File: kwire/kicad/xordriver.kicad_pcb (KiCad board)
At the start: 2 copper layers, 86.4 x 44.5 mm, 50 parts, among them J101 CONN_01X02, Q201 PMOS, Q202 NMOS, Q203 PMOS, Q204 NMOS, Q205 PMOS, Q206 NMOS, Q401 PMOS, Q402 NMOS, Q403 NMOS, Q404 PMOS, Q501 PMOS, Q502 NMOS, Q503 NMOS, Q504 PMOS, Q601 PMOS, Q602 NMOS, Q603 NMOS, Q604 PMOS, Q801 PMOS, Q802 NMOS, Q803 PMOS, Q804 NMOS, Q805 PMOS, Q806 NMOS, Q901 PMOS, Q902 NMOS, Q903 PMOS, Q904 NMOS, Q905 PMOS, Q906 NMOS

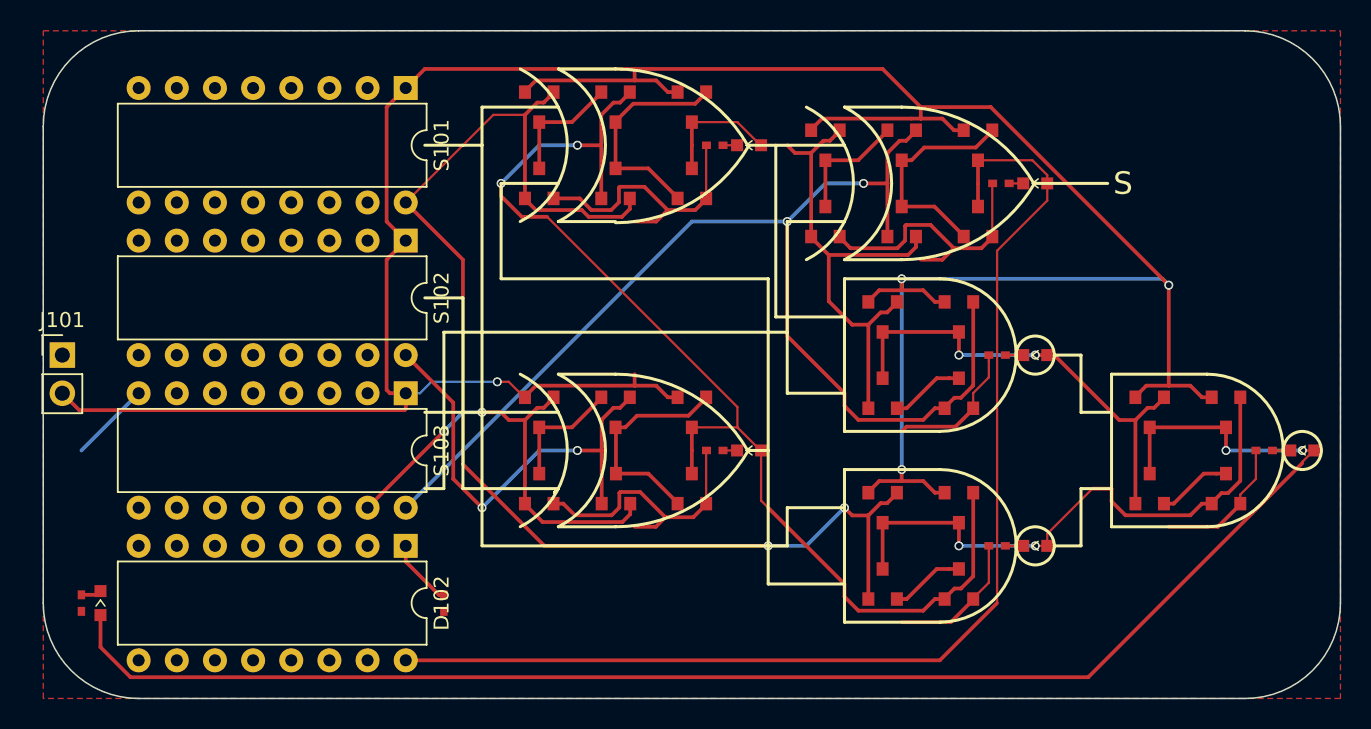
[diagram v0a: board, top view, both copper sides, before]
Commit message: Adding start for parser for kicad_pcb files
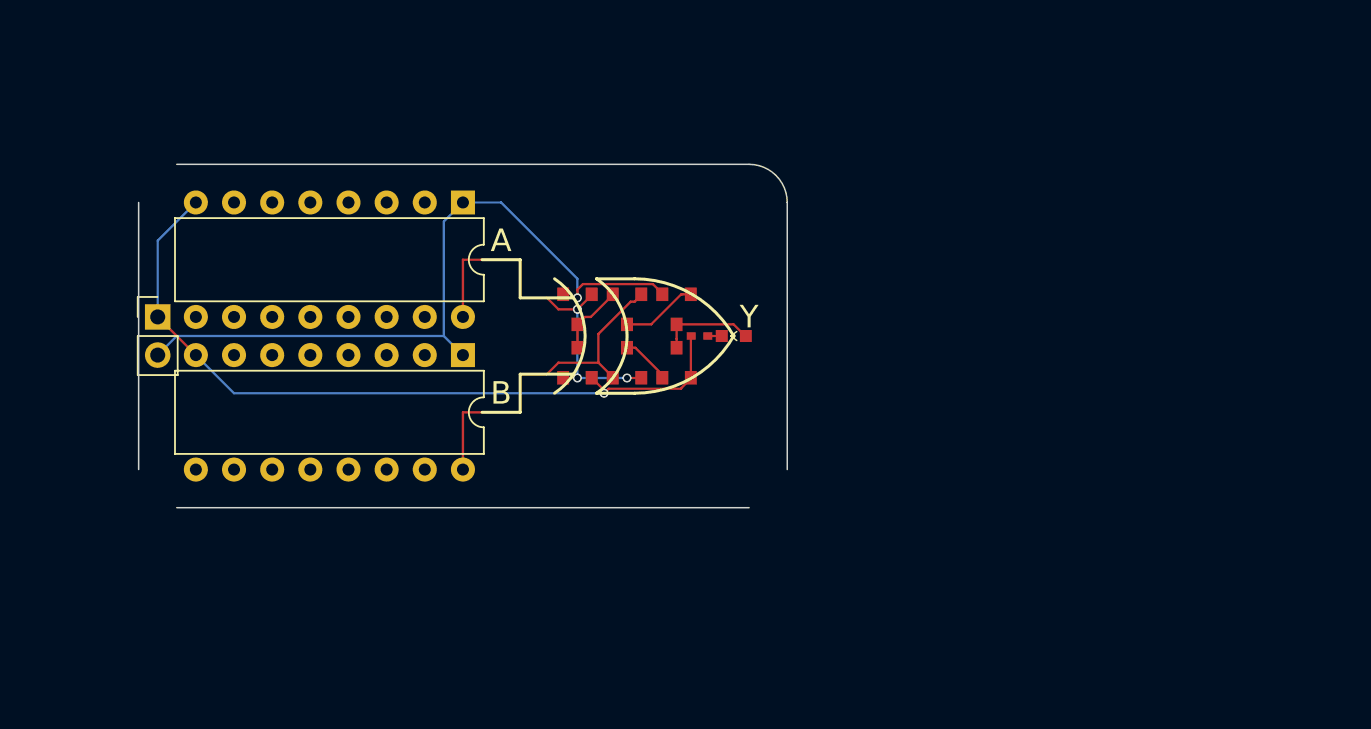
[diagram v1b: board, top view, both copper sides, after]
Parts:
- removed D101: Y, KwanSystems:D_0603
- removed D102: S, Housings_DIP:DIP-16_W7.62mm
- removed D401, D501, D601, D801, D901: LED_Small, KwanSystems:D_0603
- removed Q401, Q404, Q501, Q504, Q601, Q604, Q801, Q803, Q805, Q901, Q903, Q905: PMOS, KwanSystems:SOT-23
- removed Q402, Q403, Q502, Q503, Q602, Q603, Q802, Q804, Q806, Q902, Q904, Q906: NMOS, KwanSystems:SOT-23
- removed R101, R102, R401, R501, R601, R801, R901: RESISTOR, KwanSystems:SMD_0402
- removed S103: C, Housings_DIP:DIP-16_W7.62mm
- D201: value LED_Small -> Y
- moved Q201 13.7 mm to (105.4, 63.0)
- moved Q205 13.5 mm to (112.0, 63.0)
- moved Q203 13.5 mm to (108.7, 63.0)
- moved D201 12.7 mm to (115.8, 64.8)
- moved R201 12.7 mm to (113.5, 64.8)
- moved Q202 12.2 mm to (105.4, 66.5)
- moved Q206 12.0 mm to (112.0, 66.5)
- moved Q204 12.0 mm to (108.7, 66.5)
- moved S101 8.52 mm to (97.8, 55.9)
- moved S102 8.52 mm to (97.8, 66.0)
- moved J101 6.84 mm to (77.5, 63.5)
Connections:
- net /Y renamed /bit0/Y
- net Net-(D201-Pad1) renamed /bit0/Y-
- net Net-(Q201-Pad3) renamed /bit0/#A
- net Net-(Q203-Pad3) renamed /bit0/#Y
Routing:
- net VCC: track 204.3 -> 49.6 mm, vias 4 -> 1
- net /K: track 105.7 -> 0.00 mm, vias 2 -> 0
- net /S: track 78.9 -> 0.00 mm
- net /C: track 78.5 -> 0.00 mm, vias 2 -> 0
- net /bit0/adder/B: track 75.5 -> 0.00 mm, vias 2 -> 0
- net /A: track 84.6 -> 25.5 mm, vias 2 -> 3
- net /bit0/adder/AxorB: track 42.9 -> 0.00 mm
- net GND: track 89.8 -> 50.9 mm, vias 0 -> 1
- net /bit0/adder/#AandB: track 38.2 -> 0.00 mm, vias 2 -> 0
- net /bit0/adder/#AxorBandC: track 31.8 -> 0.00 mm, vias 2 -> 0
- net /SUB: track 29.9 -> 0.00 mm, vias 2 -> 0
- net Net-(Q803-Pad3): track 15.0 -> 0.00 mm
- net Net-(Q903-Pad3): track 14.9 -> 0.00 mm
- net Net-(Q901-Pad3): track 8.07 -> 0.00 mm
- net Net-(Q801-Pad3): track 8.07 -> 0.00 mm
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- removed copper zone on F.Cu, net GND
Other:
- board size 86.4 x 44.5 mm -> 43.2 x 22.9 mm
- board text added: "A"
- board text added: "B"
- board text added: "Y"
- board text removed: "S"

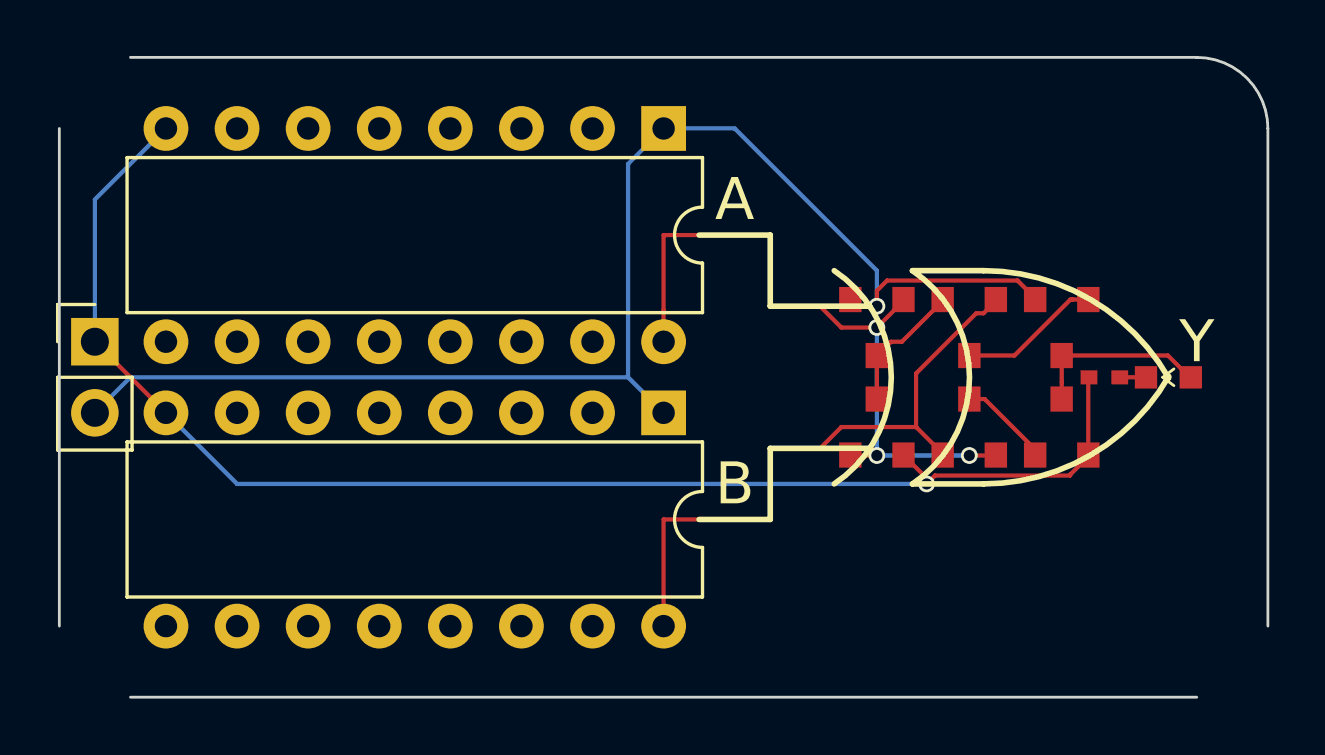
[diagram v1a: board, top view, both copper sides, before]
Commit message: Forked the XOR.
The 6-transistor XOR gate works fine, but depends on having access to the
body terminal of the transistor. In an IC, all body terminals are connected to
VCC (for PMOS) or GND (for NMOS), so that the gate voltages are relative to the
power supply rails. Therefore, you can use NMOS as a high-side switch and PMOS
as a low-side switch.

The 6T gate depends on this, because the power rails for the middle inverter are
not VCC and GND, but A and #A. When A is asserted, the middle inverter rails are
reversed from normal, and turning on the PMOS lets through low voltage instead
of the normal high voltage (and vice versa for the NMOS). You can turn on the
PMOS because the gate referenced to the body, which is tied to VCC, not to
source (and vice versa for the NMOS).

With discrete transistors, the body is always tied to the source. This means
that if you reverse the rails, you can't turn on either of the transistors,
because for the PMOS, you need the gate to be lower than the source, but the
source is low (and vice versa for the NMOS).

It is easy enough to simulate a transistor with its body wired properly -- just
ignore it. On a PMOS, the drain is set to equal the source if the gate is low,
and set to Z if the gate is high. On an NMOS, the drain is set equal to the
source if the gate is high, and Z if low.

However, a circuit built with discrete FETs won't work. As soon as the source
of the PMOS goes low, you have to hit the gate with a negative voltage (lower
than low), and as soon as the source of the NMOS goes high, you have to hit it
with a voltage higher than high.

The CD4007 chip is a set of three complementary pairs of transistors. The first
pair has its source and body pins tied to VCC and GND. The gates are connected
together and the drains are independent. The second pair has its sources
connected to pins, but its body tied to VCC and GND, respectively. The gates are
again connected together and the drains are again independent. The third pair
is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
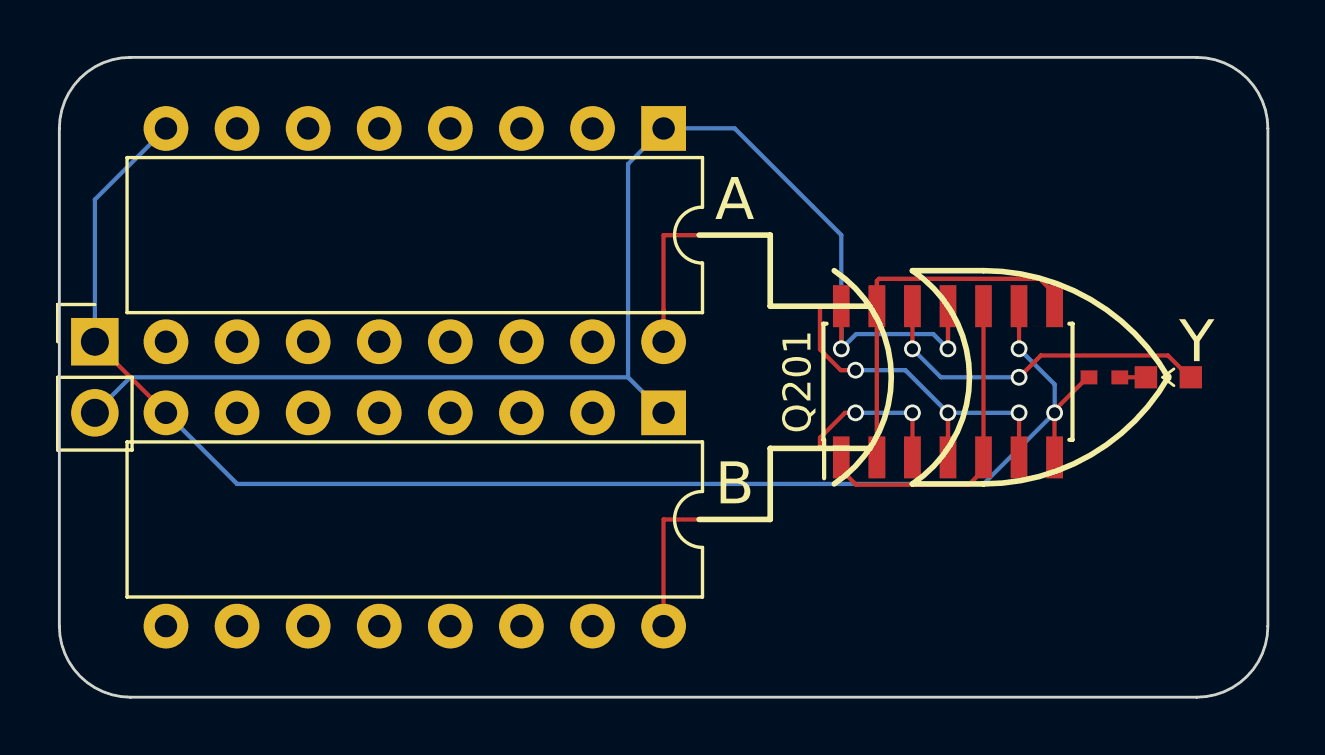
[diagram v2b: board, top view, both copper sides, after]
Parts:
- removed Q202, Q204, Q206: NMOS, KwanSystems:SOT-23
- removed Q203, Q205: PMOS, KwanSystems:SOT-23
- Q201: value PMOS -> CD4007; footprint KwanSystems:SOT-23 -> Housings_SOIC:SOIC-14_3.9x8.7mm_Pitch1.27mm
- moved Q201 3.19 mm to (108.0, 64.9), turned to 90 degrees
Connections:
- Q201 pad 1: /A -> /bit0/#Y
- Q201 pad 2: VCC -> /bit0/#A
- Q201 pad 3: /bit0/#A -> /B
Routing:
- net /bit0/#A: track 4.77 -> 13.9 mm
- net /bit0/Y: track 6.49 -> 12.5 mm, vias 0 -> 2
- net /B: track 23.0 -> 17.6 mm, vias 0 -> 2
- net GND: track 50.9 -> 53.9 mm, vias 1 -> 2
- net /bit0/#Y: track 10.1 -> 11.8 mm
- net /A: track 25.5 -> 24.8 mm
- net VCC: track 49.6 -> 50.1 mm, vias 1 -> 2

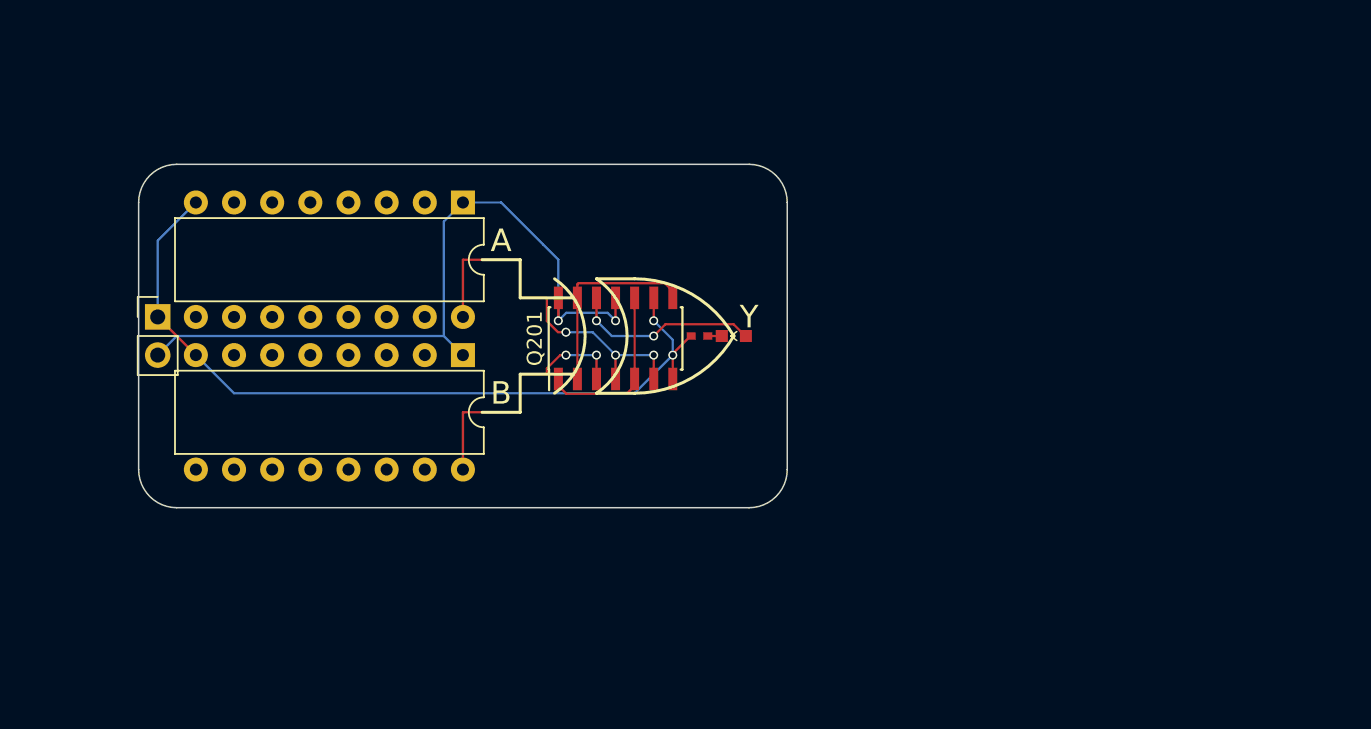
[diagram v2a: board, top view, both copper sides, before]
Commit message: Putting in gray code input enumerator
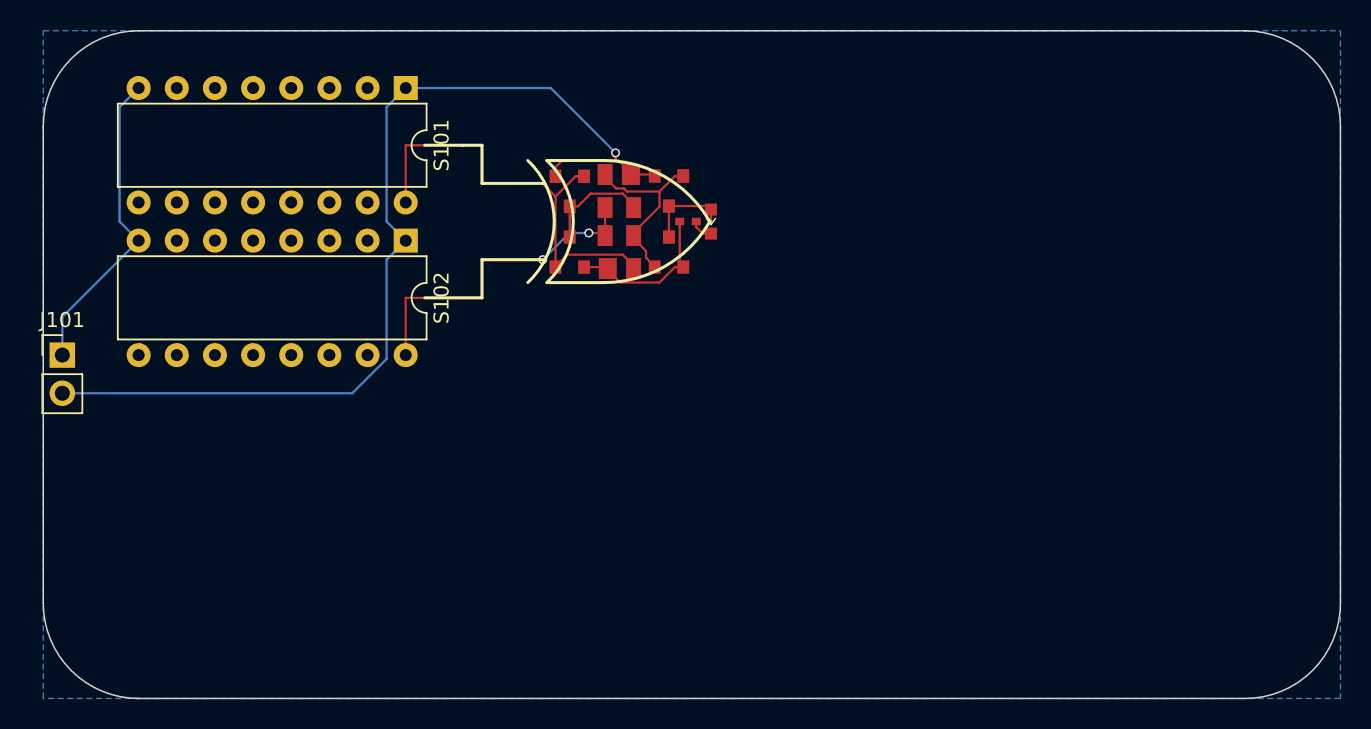
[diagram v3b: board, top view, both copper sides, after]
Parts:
- added Q202: NMOS, KwanSystems:SOT-23, F.Cu at (104.9, 59.2)
- added Q203: PMOS_BODY, KwanSystems:SOT-143, F.Cu at (108.2, 55.1)
- added Q204: NMOS_BODY, KwanSystems:SOT-143, F.Cu at (108.2, 59.2)
- added Q205: PMOS, KwanSystems:SOT-23, F.Cu at (111.5, 55.1)
- added Q206: NMOS, KwanSystems:SOT-23, F.Cu at (111.5, 59.2)
- Q201: value CD4007 -> PMOS; footprint Housings_SOIC:SOIC-14_3.9x8.7mm_Pitch1.27mm -> KwanSystems:SOT-23
- moved Q201 10.3 mm to (104.9, 55.1), turned to 270 degrees
- moved S101 8.52 mm to (94.0, 48.3)
- moved S102 8.52 mm to (94.0, 58.4)
- moved D201 7.77 mm to (114.3, 57.1), turned to 90 degrees
- moved R201 7.66 mm to (112.8, 57.1)
- moved J101 6.84 mm to (71.1, 66.0)
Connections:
- Q201 pad 1: /bit0/#Y -> /A
- Q201 pad 2: /bit0/#A -> VCC
- Q201 pad 3: /B -> /bit0/#A
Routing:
- net GND: track 53.9 -> 31.6 mm, vias 2 -> 0
- net VCC: track 50.1 -> 66.4 mm, vias 2 -> 1
- net /bit0/Y: track 12.5 -> 5.75 mm, vias 2 -> 0
- net /bit0/#A: track 13.9 -> 7.15 mm
- net /A: track 24.8 -> 29.9 mm, vias 3 -> 0
- net /B: track 17.6 -> 22.3 mm
- net /bit0/#Y: track 11.8 -> 12.5 mm
- net /bit0/Y-: track 0.94 -> 1.53 mm
- added copper zone on B.Cu, net GND
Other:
- board size 43.2 x 22.9 mm -> 86.4 x 44.5 mm
- board text removed: "A"
- board text removed: "B"
- board text removed: "Y"
